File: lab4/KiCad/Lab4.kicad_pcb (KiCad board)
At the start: 2 copper layers, 120 x 234 mm, 292 parts, among them J1 Sense test points, J10 CAN A isolation, J11 CAN A test, J14 CAN B isolation, J15 CAN B test, J2 Current test, J20 CAN A isolation, J21 CAN A test, J24 CAN B isolation, J25 CAN B test, J3 Current test, J30 CAN A isolation, J31 CAN A test, J34 CAN B isolation, J35 CAN B test, J40 Battery input: 1=+ 2=GND, J41 VBAT test, J42 Rail / PG / GND, J43 Rail / PG / GND, J44 Rail / PG / GND, J500 BOOT recovery, J501 SWD (2.54mm), J502 3.3V TTL UART, J503 LAB3 rows 1-13, J504 Additional probes, J505 Reserved / encoder probes, J550 FRONT LEFT lamp, J551 FRONT RIGHT lamp, J600 BOOT recovery, J601 SWD (2.54mm), J602 3.3V TTL UART, J603 LAB3 rows 1-13, J604 Additional probes, J605 Reserved / encoder probes, J650 REAR LEFT lamp, J651 REAR RIGHT lamp, J70 Raspberry Pi4 GPIO, J703 LAB3 rows 1-13, J704 Pi extra probes, J80 LEFT motor, J81 RIGHT motor, J82 LEFT encoder, J83 RIGHT encoder, J90 Servo: GND / 6.6V / PWM, Q1 DMPH3010LK3-13, Q550 MMBT3904, Q551 MMBT3904, Q650 MMBT3904, Q651 MMBT3904, SW50 SWT0210-045026GSA, SW51 SWT0210-045026GSA, SW60 SWT0210-045026GSA, SW61 SWT0210-045026GSA, SW70 SWT0210-045026GSA, U1 INA180A2IDBVR, U10 MCP2515T-I/ST, U11 SN65HVD231DR, U14 MCP2515T-I/ST, U15 SN65HVD231DR, U2 ACS712ELCTR-05B-T, U20 MCP2515T-I/ST, U21 SN65HVD231DR, U24 MCP2515T-I/ST, U25 SN65HVD231DR, U3 ACS712ELCTR-05B-T, U30 MCP2515T-I/ST, U31 SN65HVD231DR, U34 MCP2515T-I/ST, U35 SN65HVD231DR, U40 TPS564252DRLR, U41 TPS564252DRLR, U42 TPS564252DRLR, U50 STM32F401RET6TR, U60 STM32F401RET6TR, U80 L298N, U81 SN74LVC14APWR, Y10 16 MHz, Y14 16 MHz, Y20 16 MHz, Y24 16 MHz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

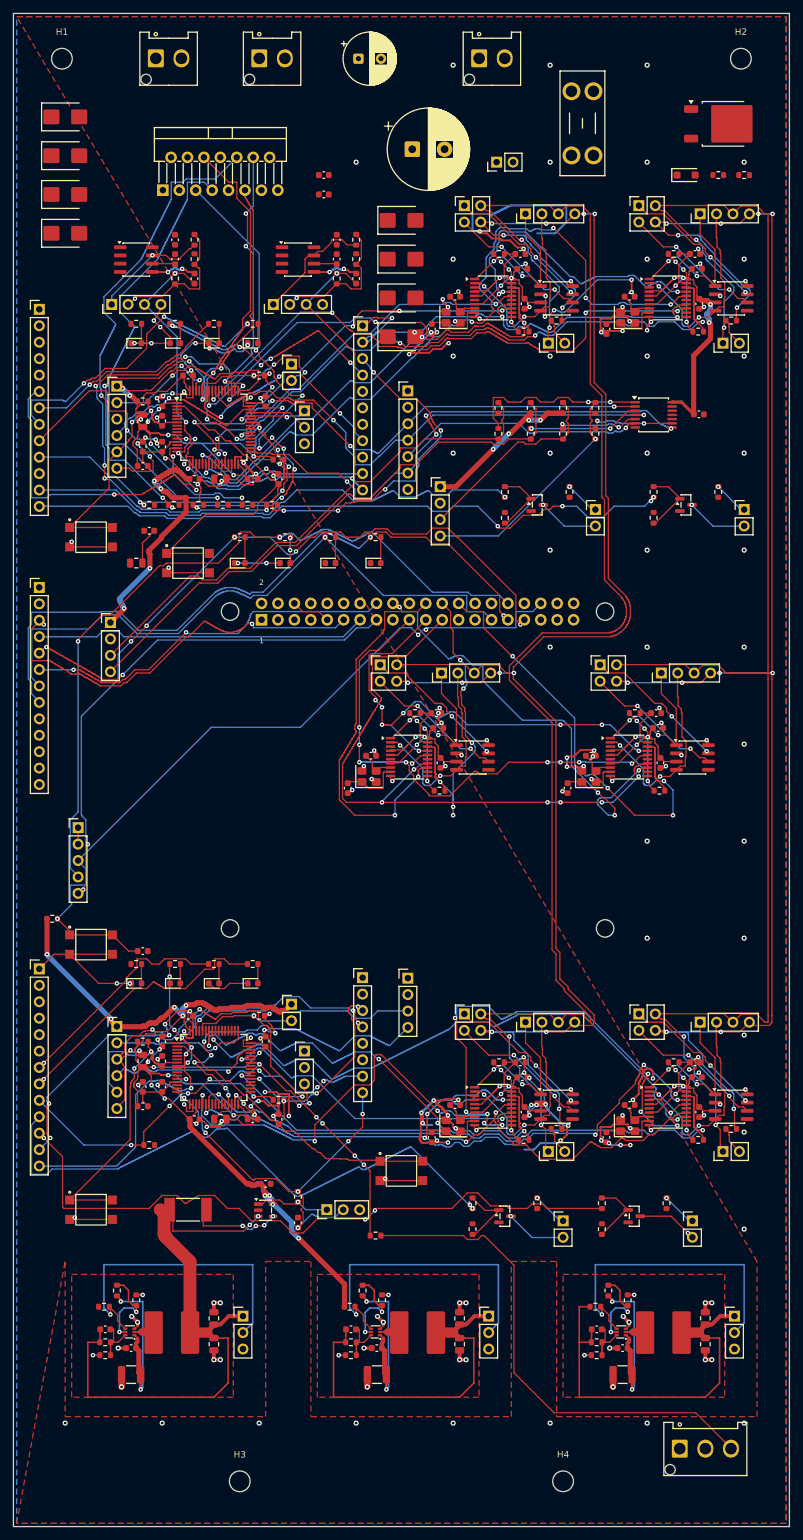
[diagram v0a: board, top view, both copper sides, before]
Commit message: Route four MCU signals and repair ground continuity
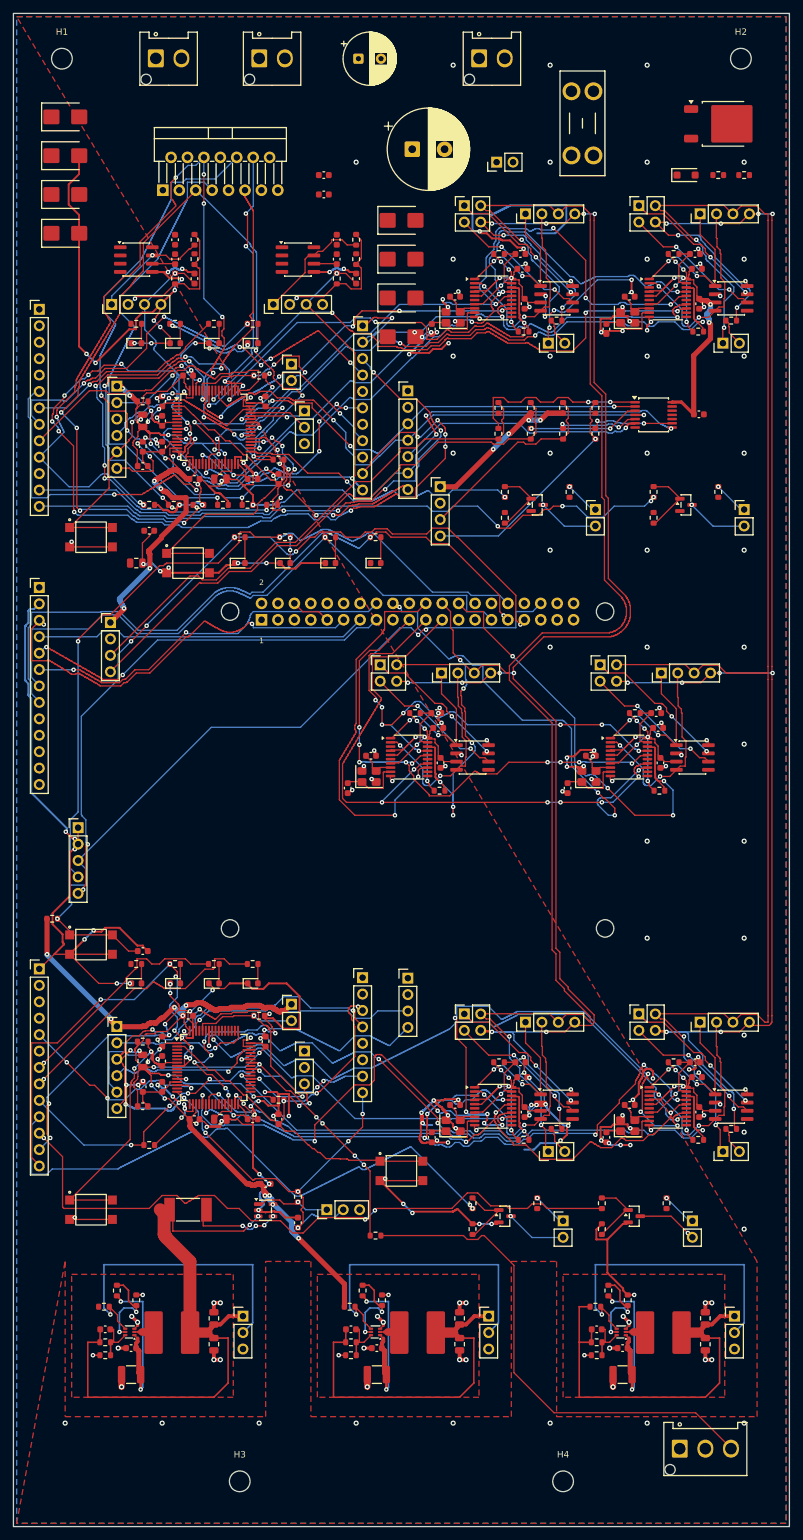
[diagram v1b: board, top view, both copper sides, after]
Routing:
- net /GND: track 639.5 -> 949.0 mm, vias 237 -> 269
- net /Rear zone/LEFT_ADC: track 70.7 -> 183.9 mm, vias 3 -> 15
- net /Rear zone/R_LEFT_IN1: track 81.5 -> 133.3 mm
- net /Rear zone/R_STEER_TASK_MARKER: track 0.00 -> 49.4 mm, vias 0 -> 5
- net /Rear zone/R_RELAY_TX_MARKER: track 0.00 -> 35.5 mm, vias 0 -> 4
- net /Front zone/F_TX_A_MARKER: track 0.00 -> 32.0 mm, vias 0 -> 3
- net /Rear zone/R_LEFT_ENABLE_PWM: track 116.6 -> 140.8 mm, vias 9 -> 11
- net /Rear zone/R_RIGHT_IN3: track 82.9 -> 105.0 mm, vias 3 -> 8
- net /Front zone/F_ERROR_LED: track 99.2 -> 108.3 mm

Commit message: Move Lab 4 routing to four layers and connect twelve MCU nets
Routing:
- net /Rear zone/R_OVERLOAD_MARKER: track 0.00 -> 76.6 mm, vias 0 -> 3
- net /Rear zone/R_STATUS_LED: track 0.00 -> 69.8 mm, vias 0 -> 4
- net /Front zone/F_DEG_A_LED: track 35.3 -> 79.0 mm, vias 1 -> 5
- net /+3V3: track 726.6 -> 768.6 mm, vias 74 -> 77
- net /Rear zone/R_DIR_A_MARKER: track 0.00 -> 39.2 mm, vias 0 -> 1
- net /Front zone/F_TX_B_MARKER: track 0.00 -> 37.2 mm, vias 0 -> 5
- net /Rear zone/R_LEFT_IN2: track 73.1 -> 109.9 mm, vias 1 -> 3
- net /Front zone/F_FRONT_RIGHT_LED: track 105.1 -> 139.9 mm, vias 3 -> 4
- net /Front zone/F_RX_A_MARKER: track 0.00 -> 33.2 mm, vias 0 -> 3
- net /Front zone/F_STEER_TASK_MARKER: track 0.00 -> 32.8 mm, vias 0 -> 1
- net /Rear zone/R_PID_MARKER: track 0.00 -> 28.9 mm, vias 0 -> 3
- net /Front zone/F_STATUS_LED: track 0.00 -> 23.4 mm, vias 0 -> 2
- net /Rear zone/R_RIGHT_IN4: track 116.3 -> 94.9 mm, vias 10 -> 4
- net /Rear zone/R_TASK_PROBE: track 0.00 -> 20.9 mm, vias 0 -> 1
- net /GND: track 949.0 -> 952.3 mm
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- added copper zone on In1.Cu, net /GND
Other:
- copper layers 2 -> 4
